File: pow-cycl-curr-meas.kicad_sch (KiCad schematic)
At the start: 62 parts, among them Q1 SQS401EN-T1_BE3, Q10 SSM3K15ACT, Q2 SQS401EN-T1_BE3, Q3 SSM3K15ACT, Q4 SSM3K15ACT, Q5 SQS401EN-T1_BE3, Q6 SSM3K15ACT, Q7 SQS401EN-T1_BE3, Q8 SQS401EN-T1_BE3, Q9 SSM3K15ACT, U10 TCA9534, U11 TMCS1100A2-Q1, U12 TMCS1100A2-Q1, U13 TMCS1100A2-Q1, U14 ADS7828, U8 TMCS1100A2-Q1, U9 TMCS1100A2-Q1

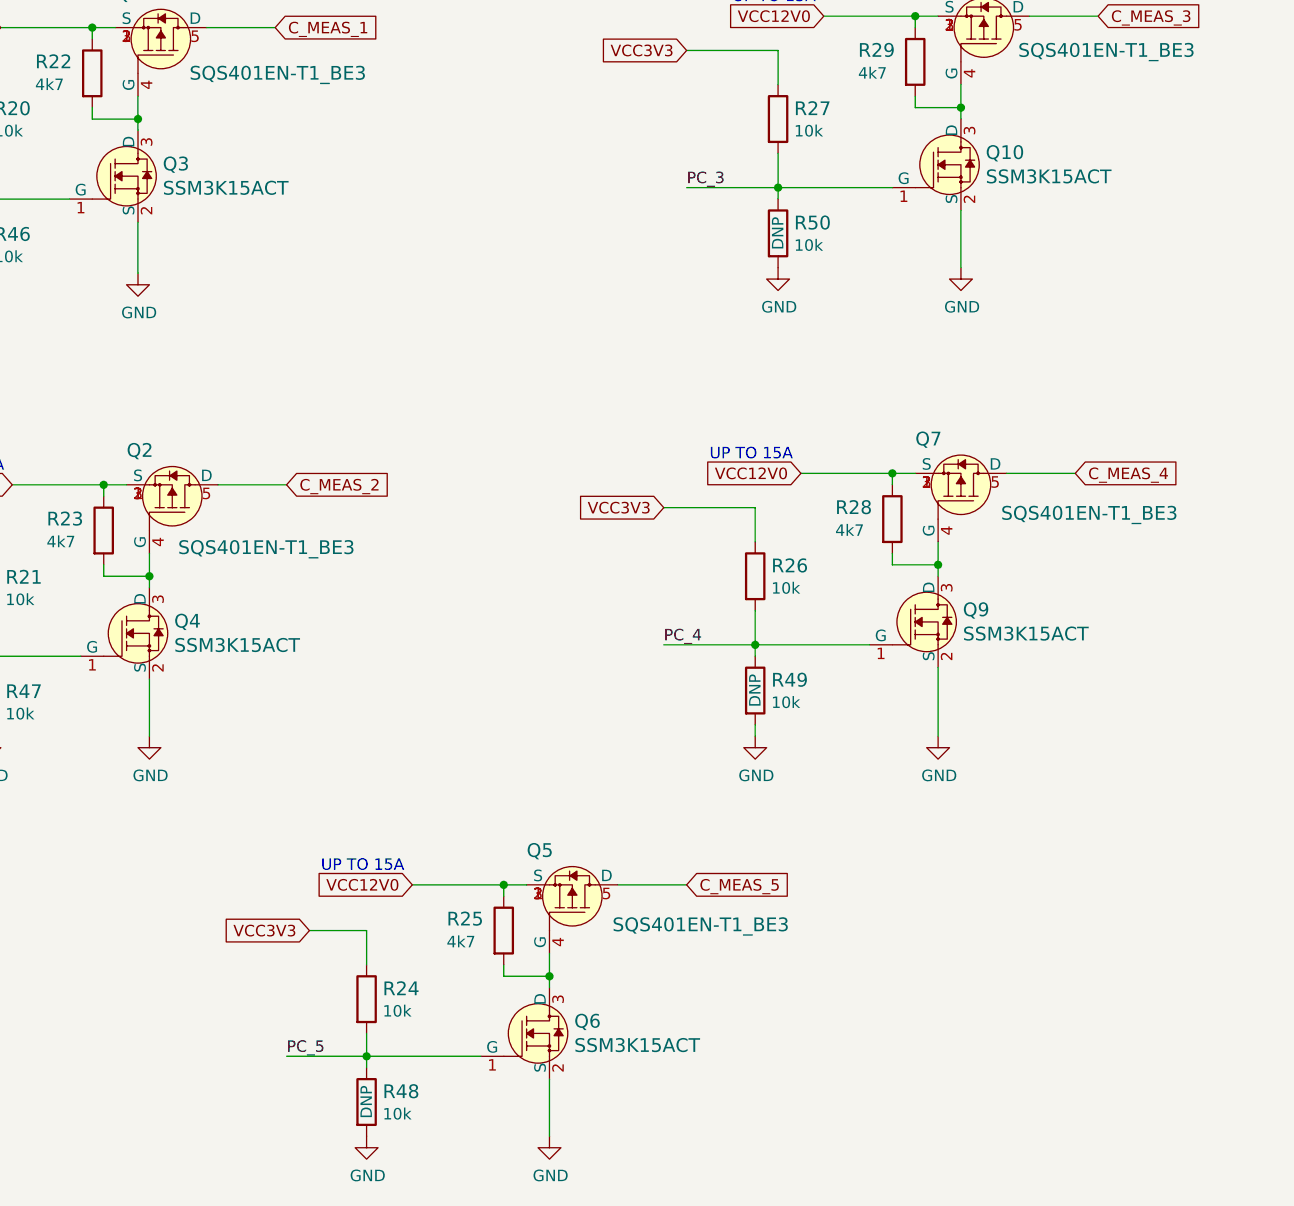
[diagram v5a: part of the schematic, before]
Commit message: Replaced transistors with larger package
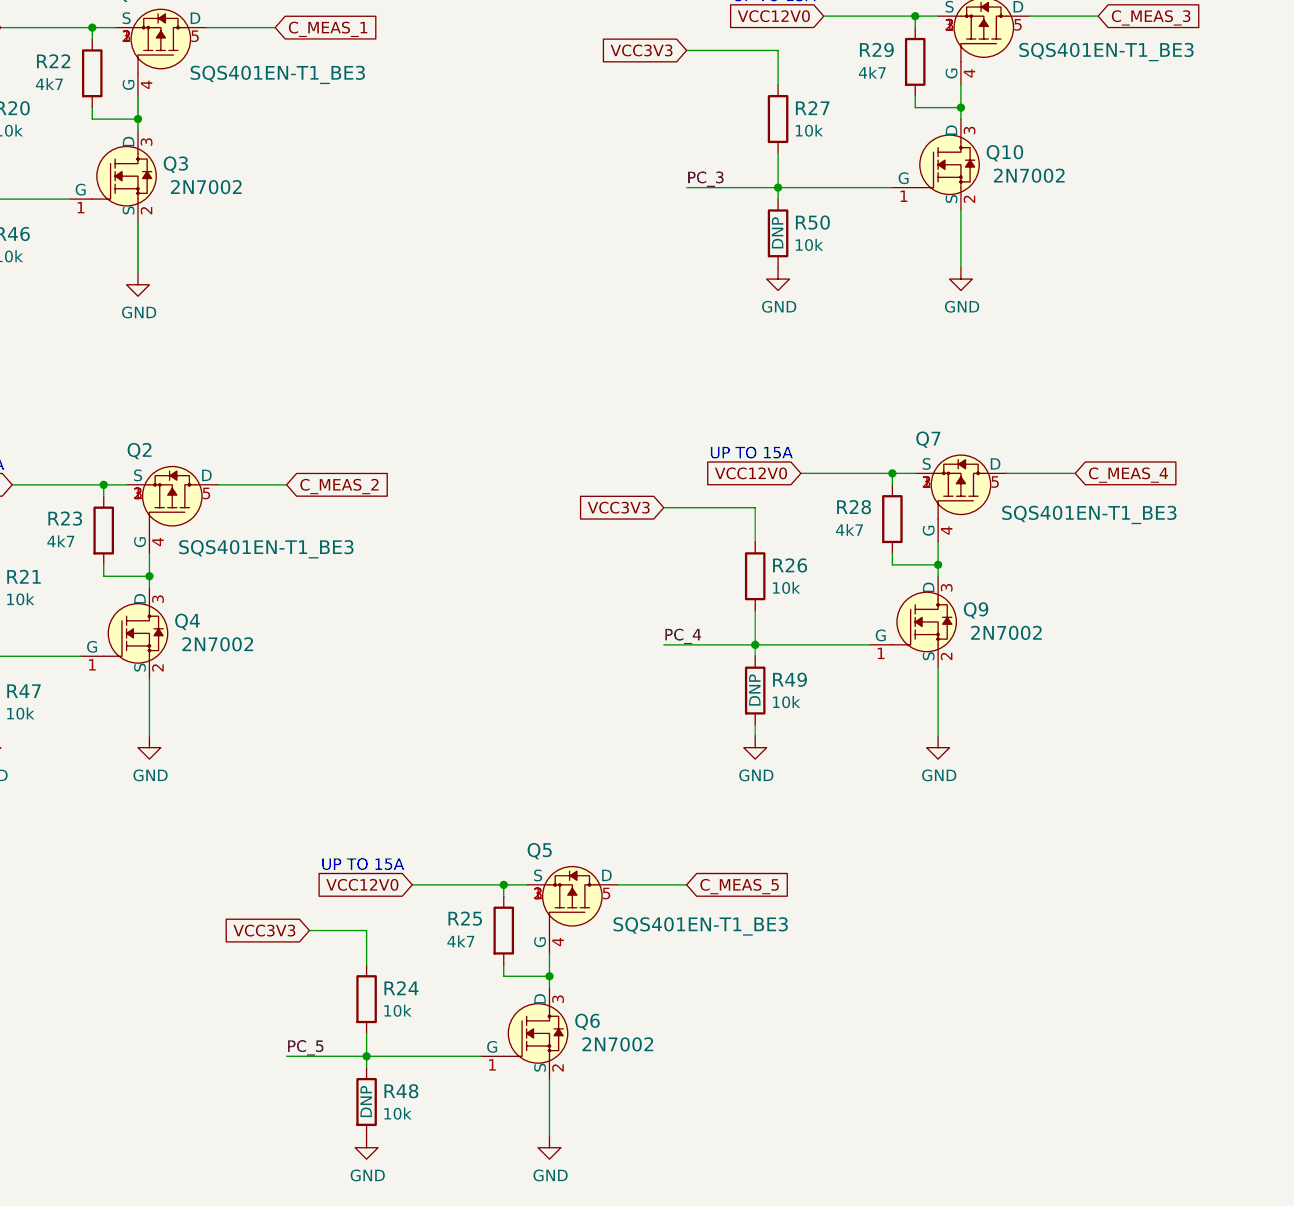
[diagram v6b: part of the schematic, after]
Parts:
- Q10, Q3, Q4, Q6, Q9: value SSM3K15ACT -> 2N7002; footprint nuc-compute-cluster-power-breakout-footprints:SSM3K15ACT -> antmicro-footprints:SOT-23-3; symbol nuc-compute-cluster-power-breakout:SSM3K15ACT -> antmicroTransistorsFETsMOSFETsSingle:2N7002; MPN SSM3K15ACT,L3F -> 2N7002; Manufacturer Toshiba -> ON Semiconductor
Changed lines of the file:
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@@
     (pin "2")
   )
-  (symbol (lib_id "nuc-compute-cluster-power-breakout:SSM3K15ACT") (at 160.02 166.37 0) (unit 1)
+  (symbol (lib_id "antmicroTransistorsFETsMOSFETsSingle:2N7002") (at 160.02 166.37 0) (unit 1)
     (in_bom yes) (on_board yes)
     (property "Reference" "Q3" (id 0) (at 162.7632 165.0238 0)
       (effects (font (size 1.524 1.524)) (justify left))
     )
-    (property "Value" "SSM3K15ACT" (id 1) (at 162.7632 167.7162 0)
-      (effects (font (size 1.524 1.524)) (justify left))
-    )
-    (property "Footprint" "nuc-compute-cluster-power-breakout-footprints:SSM3K15ACT" (id 2) (at 148.59 161.29 0)
-      (effects (font (size 1.524 1.524)) hide)
-    )
-    (property "Datasheet" "https://www.mouser.pl/datasheet/2/408/SSM3K15ACT_datasheet_en_20140301-1144185.pdf" (id 3) (at 130.81 153.67 0)
-      (effects (font (size 1.524 1.524)) hide)
-    )
-    (property "MPN" "SSM3K15ACT,L3F " (id 4) (at 160.02 166.37 0)
-      (effects (font (size 1.27 1.27)) hide)
-    )
-    (property "Manufacturer" "Toshiba" (id 5) (at 160.02 166.37 0)
-      (effects (font (size 1.27 1.27)) hide)
+    (property "Value" "2N7002" (id 1) (at 167.64 167.64 0)
+      (effects (font (size 1.524 1.524)))
+    )
+    (property "Footprint" "antmicro-footprints:SOT-23-3" (id 2) (at 165.1 161.29 0)
+      (effects (font (size 1.524 1.524)) (justify left) hide)
+    )
+    (property "Datasheet" "https://www.onsemi.com/pub/Collateral/NDS7002A-D.PDF" (id 3) (at 165.1 158.75 0)
+      (effects (font (size 1.524 1.524)) (justify left) hide)
+    )
+    (property "MPN" "2N7002" (id 4) (at 165.1 153.67 0)
+      (effects (font (size 1.524 1.524)) (justify left) hide)
+    )
+    (property "Manufacturer" "ON Semiconductor" (id 5) (at 165.1 138.43 0)
+      (effects (font (size 1.524 1.524)) (justify left) hide)
     )
     (pin "1")
@@
     (pin "1")
   )
-  (symbol (lib_id "nuc-compute-cluster-power-breakout:SSM3K15ACT") (at 205.74 261.62 0) (unit 1)
+  (symbol (lib_id "antmicroTransistorsFETsMOSFETsSingle:2N7002") (at 205.74 261.62 0) (unit 1)
     (in_bom yes) (on_board yes)
     (property "Reference" "Q6" (id 0) (at 208.4832 260.2738 0)
       (effects (font (size 1.524 1.524)) (justify left))
     )
-    (property "Value" "SSM3K15ACT" (id 1) (at 208.4832 262.9662 0)
-      (effects (font (size 1.524 1.524)) (justify left))
-    )
-    (property "Footprint" "nuc-compute-cluster-power-breakout-footprints:SSM3K15ACT" (id 2) (at 194.31 256.54 0)
-      (effects (font (size 1.524 1.524)) hide)
-    )
-    (property "Datasheet" "https://www.mouser.pl/datasheet/2/408/SSM3K15ACT_datasheet_en_20140301-1144185.pdf" (id 3) (at 176.53 248.92 0)
-      (effects (font (size 1.524 1.524)) hide)
-    )
-    (property "MPN" "SSM3K15ACT,L3F " (id 4) (at 205.74 261.62 0)
-      (effects (font (size 1.27 1.27)) hide)
-    )
-    (property "Manufacturer" "Toshiba" (id 5) (at 205.74 261.62 0)
-      (effects (font (size 1.27 1.27)) hide)
+    (property "Value" "2N7002" (id 1) (at 213.36 262.89 0)
+      (effects (font (size 1.524 1.524)))
+    )
+    (property "Footprint" "antmicro-footprints:SOT-23-3" (id 2) (at 210.82 256.54 0)
+      (effects (font (size 1.524 1.524)) (justify left) hide)
+    )
+    (property "Datasheet" "https://www.onsemi.com/pub/Collateral/NDS7002A-D.PDF" (id 3) (at 210.82 254 0)
+      (effects (font (size 1.524 1.524)) (justify left) hide)
+    )
+    (property "MPN" "2N7002" (id 4) (at 210.82 248.92 0)
+      (effects (font (size 1.524 1.524)) (justify left) hide)
+    )
+    (property "Manufacturer" "ON Semiconductor" (id 5) (at 210.82 233.68 0)
+      (effects (font (size 1.524 1.524)) (justify left) hide)
     )
     (pin "1")
@@
     (pin "1")
   )
-  (symbol (lib_id "nuc-compute-cluster-power-breakout:SSM3K15ACT") (at 161.29 217.17 0) (unit 1)
+  (symbol (lib_id "antmicroTransistorsFETsMOSFETsSingle:2N7002") (at 161.29 217.17 0) (unit 1)
     (in_bom yes) (on_board yes)
     (property "Reference" "Q4" (id 0) (at 164.0332 215.8238 0)
       (effects (font (size 1.524 1.524)) (justify left))
     )
-    (property "Value" "SSM3K15ACT" (id 1) (at 164.0332 218.5162 0)
-      (effects (font (size 1.524 1.524)) (justify left))
-    )
-    (property "Footprint" "nuc-compute-cluster-power-breakout-footprints:SSM3K15ACT" (id 2) (at 149.86 212.09 0)
-      (effects (font (size 1.524 1.524)) hide)
-    )
-    (property "Datasheet" "https://www.mouser.pl/datasheet/2/408/SSM3K15ACT_datasheet_en_20140301-1144185.pdf" (id 3) (at 132.08 204.47 0)
-      (effects (font (size 1.524 1.524)) hide)
-    )
-    (property "MPN" "SSM3K15ACT,L3F " (id 4) (at 161.29 217.17 0)
-      (effects (font (size 1.27 1.27)) hide)
-    )
-    (property "Manufacturer" "Toshiba" (id 5) (at 161.29 217.17 0)
-      (effects (font (size 1.27 1.27)) hide)
+    (property "Value" "2N7002" (id 1) (at 168.91 218.44 0)
+      (effects (font (size 1.524 1.524)))
+    )
+    (property "Footprint" "antmicro-footprints:SOT-23-3" (id 2) (at 166.37 212.09 0)
+      (effects (font (size 1.524 1.524)) (justify left) hide)
+    )
+    (property "Datasheet" "https://www.onsemi.com/pub/Collateral/NDS7002A-D.PDF" (id 3) (at 166.37 209.55 0)
+      (effects (font (size 1.524 1.524)) (justify left) hide)
+    )
+    (property "MPN" "2N7002" (id 4) (at 166.37 204.47 0)
+      (effects (font (size 1.524 1.524)) (justify left) hide)
+    )
+    (property "Manufacturer" "ON Semiconductor" (id 5) (at 166.37 189.23 0)
+      (effects (font (size 1.524 1.524)) (justify left) hide)
     )
     (pin "1")
@@
     (pin "1")
   )
-  (symbol (lib_id "nuc-compute-cluster-power-breakout:SSM3K15ACT") (at 251.46 165.1 0) (unit 1)
+  (symbol (lib_id "antmicroTransistorsFETsMOSFETsSingle:2N7002") (at 251.46 165.1 0) (unit 1)
     (in_bom yes) (on_board yes)
     (property "Reference" "Q10" (id 0) (at 254.2032 163.7538 0)
       (effects (font (size 1.524 1.524)) (justify left))
     )
-    (property "Value" "SSM3K15ACT" (id 1) (at 254.2032 166.4462 0)
-      (effects (font (size 1.524 1.524)) (justify left))
-    )
-    (property "Footprint" "nuc-compute-cluster-power-breakout-footprints:SSM3K15ACT" (id 2) (at 240.03 160.02 0)
-      (effects (font (size 1.524 1.524)) hide)
-    )
-    (property "Datasheet" "https://www.mouser.pl/datasheet/2/408/SSM3K15ACT_datasheet_en_20140301-1144185.pdf" (id 3) (at 222.25 152.4 0)
-      (effects (font (size 1.524 1.524)) hide)
-    )
-    (property "MPN" "SSM3K15ACT,L3F " (id 4) (at 251.46 165.1 0)
-      (effects (font (size 1.27 1.27)) hide)
-    )
-    (property "Manufacturer" "Toshiba" (id 5) (at 251.46 165.1 0)
-      (effects (font (size 1.27 1.27)) hide)
+    (property "Value" "2N7002" (id 1) (at 259.08 166.37 0)
+      (effects (font (size 1.524 1.524)))
+    )
+    (property "Footprint" "antmicro-footprints:SOT-23-3" (id 2) (at 256.54 160.02 0)
+      (effects (font (size 1.524 1.524)) (justify left) hide)
+    )
+    (property "Datasheet" "https://www.onsemi.com/pub/Collateral/NDS7002A-D.PDF" (id 3) (at 256.54 157.48 0)
+      (effects (font (size 1.524 1.524)) (justify left) hide)
+    )
+    (property "MPN" "2N7002" (id 4) (at 256.54 152.4 0)
+      (effects (font (size 1.524 1.524)) (justify left) hide)
+    )
+    (property "Manufacturer" "ON Semiconductor" (id 5) (at 256.54 137.16 0)
+      (effects (font (size 1.524 1.524)) (justify left) hide)
     )
     (pin "1")
@@
     (pin "1")
   )
-  (symbol (lib_id "nuc-compute-cluster-power-breakout:SSM3K15ACT") (at 248.92 215.9 0) (unit 1)
+  (symbol (lib_id "antmicroTransistorsFETsMOSFETsSingle:2N7002") (at 248.92 215.9 0) (unit 1)
     (in_bom yes) (on_board yes)
     (property "Reference" "Q9" (id 0) (at 251.6632 214.5538 0)
       (effects (font (size 1.524 1.524)) (justify left))
     )
-    (property "Value" "SSM3K15ACT" (id 1) (at 251.6632 217.2462 0)
-      (effects (font (size 1.524 1.524)) (justify left))
-    )
-    (property "Footprint" "nuc-compute-cluster-power-breakout-footprints:SSM3K15ACT" (id 2) (at 237.49 210.82 0)
-      (effects (font (size 1.524 1.524)) hide)
-    )
-    (property "Datasheet" "https://www.mouser.pl/datasheet/2/408/SSM3K15ACT_datasheet_en_20140301-1144185.pdf" (id 3) (at 219.71 203.2 0)
-      (effects (font (size 1.524 1.524)) hide)
-    )
-    (property "MPN" "SSM3K15ACT,L3F " (id 4) (at 248.92 215.9 0)
-      (effects (font (size 1.27 1.27)) hide)
-    )
-    (property "Manufacturer" "Toshiba" (id 5) (at 248.92 215.9 0)
-      (effects (font (size 1.27 1.27)) hide)
-    )
-    (pin "1")
+    (property "Value" "2N7002" (id 1) (at 256.54 217.17 0)
+      (effects (font (size 1.524 1.524)))
+    )
+    (property "Footprint" "antmicro-footprints:SOT-23-3" (id 2) (at 254 210.82 0)
+      (effects (font (size 1.524 1.524)) (justify left) hide)
+    )
+    (property "Datasheet" "https://www.onsemi.com/pub/Collateral/NDS7002A-D.PDF" (id 3) (at 254 208.28 0)
+      (effects (font (size 1.524 1.524)) (justify left) hide)
+    )
+    (property "MPN" "2N7002" (id 4) (at 254 203.2 0)
+      (effects (font (size 1.524 1.524)) (justify left) hide)
+    )
+    (property "Manufacturer" "ON Semiconductor" (id 5) (at 254 187.96 0)
+      (effects (font (size 1.524 1.524)) (justify left) hide)
+    )
+    (pin "1")
